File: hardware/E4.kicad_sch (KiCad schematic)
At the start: 0 parts

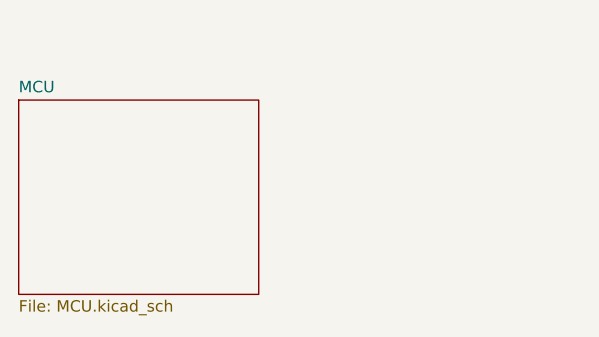
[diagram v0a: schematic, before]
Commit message: feat：仪表放大器、滤波器原理图
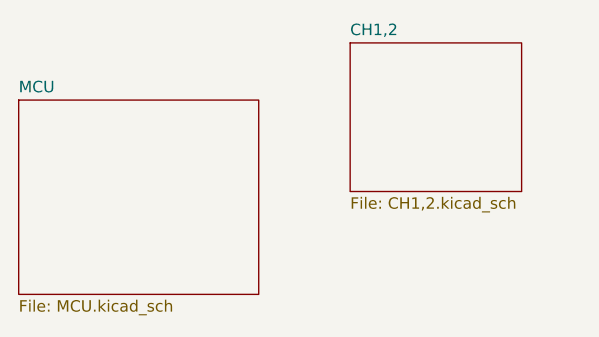
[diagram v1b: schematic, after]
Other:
- added sheet CH1,2 (CH1,2.kicad_sch)
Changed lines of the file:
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@@
 	(paper "A4")
+	(sheet
+		(at 72.39 22.86)
+		(size 19.05 16.51)
+		(exclude_from_sim no)
+		(in_bom yes)
+		(on_board yes)
+		(dnp no)
+		(fields_autoplaced yes)
+		(stroke
+			(width 0.1524)
+			(type solid)
+		)
+		(fill
+			(color 0 0 0 0)
+		)
+		(property "Sheetname" "CH1,2"
+			(at 72.39 22.1484 0)
+			(show_name no)
+			(do_not_autoplace no)
+			(effects
+				(font
+					(size 1.27 1.27)
+				)
+				(justify left bottom)
+			)
+		)
+		(property "Sheetfile" "CH1,2.kicad_sch"
+			(at 72.39 39.9546 0)
+			(show_name no)
+			(do_not_autoplace no)
+			(effects
+				(font
+					(size 1.27 1.27)
+				)
+				(justify left top)
+			)
+		)
+		(instances
+			(project "E4"
+				(path "/7664cc8d-15c4-46a0-b3f4-8b4373008b19"
+					(page "3")
+				)
+			)
+		)
+	)
 	(sheet
 		(at 35.56 29.21)
